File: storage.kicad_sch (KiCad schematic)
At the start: 39 parts, among them J6 Micro_SD_Card_Det1, U1 MIMX8MM6DVTLZAA, U25 TPD4E02B04, U26 W25Q32JWZP, U27 TPD4E02B04, U28 D5V0H1B2LP, U29 SiP32431DR3, U30 74LVC2G07, U31 EMMC

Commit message: misc changes for rev1
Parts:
- D6: value LED_Red -> LED_Blue; MPN SML-E12U8WT86 -> 150060BS55040
- R89, R92: now left out of the parts list
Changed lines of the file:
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@@
   )
   (symbol (lib_id "Device:R") (at 237.49 99.06 0) (unit 1)
-    (in_bom yes) (on_board yes)
+    (in_bom no) (on_board yes)
     (property "Reference" "R92" (id 0) (at 240.03 97.7899 0)
       (effects (font (size 1.27 1.27)) (justify left))
@@
       (effects (font (size 1.27 1.27)) (justify right))
     )
-    (property "Value" "LED_Red" (id 1) (at 327.66 44.7674 90)
+    (property "Value" "LED_Blue" (id 1) (at 327.66 44.7674 90)
       (effects (font (size 1.27 1.27)) (justify right))
     )
@@
       (effects (font (size 1.27 1.27)) hide)
     )
-    (property "MPN" "SML-E12U8WT86" (id 4) (at 323.85 41.91 0)
+    (property "MPN" "150060BS55040" (id 4) (at 323.85 41.91 0)
       (effects (font (size 1.27 1.27)) hide)
     )
@@
   )
   (symbol (lib_id "Device:R") (at 227.33 99.06 0) (unit 1)
-    (in_bom yes) (on_board yes)
+    (in_bom no) (on_board yes)
     (property "Reference" "R89" (id 0) (at 229.87 97.7899 0)
       (effects (font (size 1.27 1.27)) (justify left))

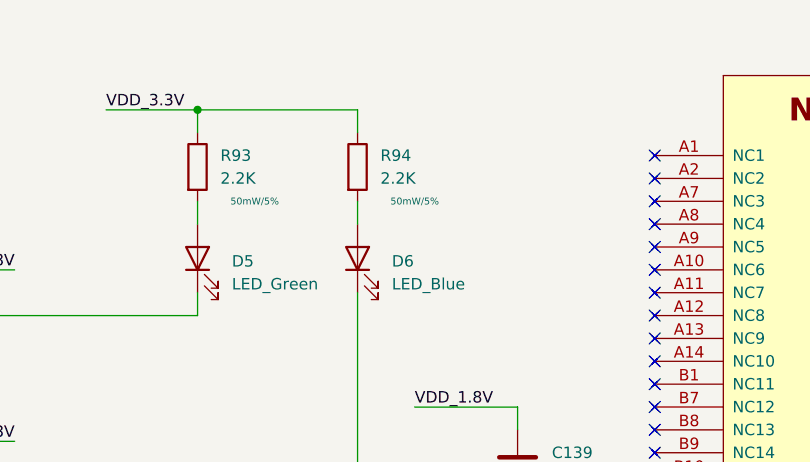
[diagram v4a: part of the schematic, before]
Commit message: fixup qwiic con p/n, fixup dnp and values based on testing
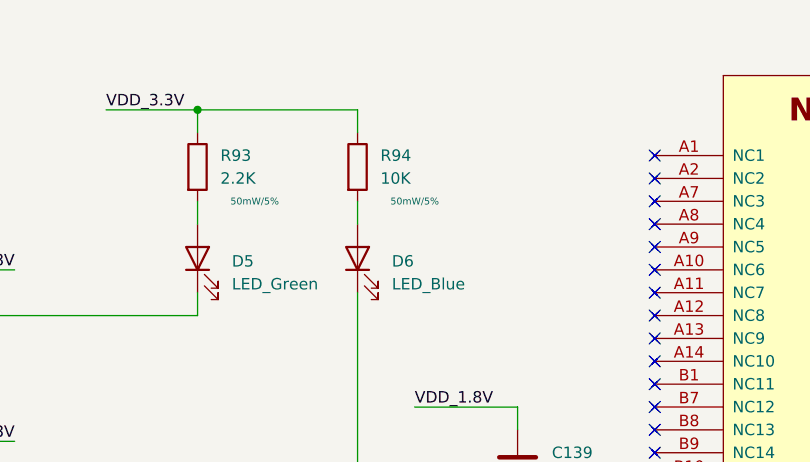
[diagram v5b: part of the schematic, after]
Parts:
- R94: value 2.2K -> 10K; MPN RC0402FR-072K2L -> RC0402FR-0710KL
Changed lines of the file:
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@@
       (effects (font (size 1.27 1.27)) (justify left))
     )
-    (property "Value" "2.2K" (id 1) (at 326.39 33.0199 0)
+    (property "Value" "10K" (id 1) (at 326.39 33.0199 0)
       (effects (font (size 1.27 1.27)) (justify left))
     )
@@
       (effects (font (size 0.762 0.762)))
     )
-    (property "MPN" "RC0402FR-072K2L" (id 5) (at 323.85 31.75 0)
+    (property "MPN" "RC0402FR-0710KL" (id 5) (at 323.85 31.75 0)
       (effects (font (size 1.27 1.27)) hide)
     )
